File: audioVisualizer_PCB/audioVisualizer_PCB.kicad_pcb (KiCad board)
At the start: 2 copper layers, 129.1 x 32.5 mm, 34 parts, among them J1 USB_C_Receptacle_USB2.0_16P, J3 SPI_LED_MATRIX, U2 HT7333, U7 STM32F401CCUx, Y1 ASE-25MHz

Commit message: reflect on code as well
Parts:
- renumbered TP2 to 3V3, TP1 to 5V1, TP5 to GND1
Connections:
- J3 pad 4: Net-(J3-CS) -> SPI_CS
- U7 pad 16: Net-(J3-CS) -> unconnected-(U7-PA6-Pad16)
- U7 pad 27: unconnected-(U7-PB14-Pad27) -> SPI_CS
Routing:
- net SPI_CS: track 0.00 -> 66.5 mm
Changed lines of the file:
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@@
 			(layers "*.Cu" "*.Mask")
 			(remove_unused_layers no)
-			(net "Net-(J3-CS)")
+			(net "SPI_CS")
 			(pinfunction "CS_4")
 			(pintype "passive")
@@
 			(layers "F.Cu" "F.Mask" "F.Paste")
 			(roundrect_rratio 0.25)
-			(net "Net-(J3-CS)")
+			(net "unconnected-(U7-PA6-Pad16)")
 			(pinfunction "PA6_16")
 			(pintype "bidirectional")
@@
 			(layers "F.Cu" "F.Mask" "F.Paste")
 			(roundrect_rratio 0.25)
-			(net "unconnected-(U7-PB14-Pad27)")
+			(net "SPI_CS")
 			(pinfunction "PB14_27")
 			(pintype "bidirectional")
@@
 		(descr "SMD rectangular pad as test Point, square 1.0mm side length")
 		(tags "test point SMD pad rectangle square")
-		(property "Reference" "TP1"
+		(property "Reference" "5V1"
 			(at 0 1.448 0)
 			(layer "B.SilkS")
@@
 		(descr "SMD rectangular pad as test Point, square 1.0mm side length")
 		(tags "test point SMD pad rectangle square")
-		(property "Reference" "TP2"
+		(property "Reference" "3V3"
 			(at 0 1.448 0)
 			(layer "B.SilkS")
@@
 		(descr "SMD rectangular pad as test Point, square 1.0mm side length")
 		(tags "test point SMD pad rectangle square")
-		(property "Reference" "TP5"
+		(property "Reference" "GND1"
 			(at 0 1.448 0)
 			(layer "B.SilkS")
@@
 	(segment
 		(start 81.6245 88.2832)
-		(end 81.6245 88.7666)
+		(end 81.6245 89.1245)
 		(width 0.2)
 		(layer "F.Cu")
@@
 	)
 	(segment
-		(start 82.8328 89.9749)
+		(start 82.4749 89.9749)
 		(end 145.6851 89.9749)
 		(width 0.2)
@@
 	)
 	(segment
-		(start 81.6245 88.7666)
-		(end 82.8328 89.9749)
+		(start 81.6245 89.1245)
+		(end 82.4749 89.9749)
 		(width 0.2)
 		(layer "F.Cu")
@@
 		(net "Net-(J1-CC2)")
 	)
+	(segment
+		(start 145.223654 83.73)
+		(end 146.176346 83.73)
+		(width 0.2)
+		(layer "F.Cu")
+		(net "SPI_CS")
+	)
+	(segment
+		(start 89.553571 88.4194)
+		(end 140.534254 88.4194)
+		(width 0.2)
+		(layer "F.Cu")
+		(net "SPI_CS")
+	)
+	(segment
+		(start 140.534254 88.4194)
+		(end 145.223654 83.73)
+		(width 0.2)
+		(layer "F.Cu")
+		(net "SPI_CS")
+	)
+	(segment
+		(start 146.176346 83.73)
+		(end 146.85 84.403654)
+		(width 0.2)
+		(layer "F.Cu")
+		(net "SPI_CS")
+	)
+	(segment
+		(start 146.85 86.27)
+		(end 145.7 87.42)
+		(width 0.2)
+		(layer "F.Cu")
+		(net "SPI_CS")
+	)
+	(segment
+		(start 87.729871 86.5957)
+		(end 89.553571 88.4194)
+		(width 0.2)
+		(layer "F.Cu")
+		(net "SPI_CS")
+	)
+	(segment
+		(start 146.85 84.403654)
+		(end 146.85 86.27)
+		(width 0.2)
+		(layer "F.Cu")
+		(net "SPI_CS")
+	)
+	(segment
+		(start 86.812 86.5957)
+		(end 87.729871 86.5957)
+		(width 0.2)
+		(layer "F.Cu")
+		(net "SPI_CS")
+	)
 	(embedded_fonts no)

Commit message: update
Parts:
- removed TP3: SWDIO, TestPoint:TestPoint_Pad_1.0x1.0mm
- removed TP4: SWCLK, TestPoint:TestPoint_Pad_1.0x1.0mm
- added D2: LED, LED_SMD:LED_0805_2012Metric, F.Cu at (48.3, 96.0)
- added J2: SWD_DEBUG, Connector_PinHeader_2.54mm:PinHeader_1x04_P2.54mm_Vertical, F.Cu at (94.1, 70.5)
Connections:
- U7 pad 34: Net-(U7-PA13) -> SWDIO
- U7 pad 37: Net-(U7-PA14) -> SWCLK
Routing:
- net +5V: track 173.9 -> 216.9 mm
- net GND: track 310.7 -> 275.9 mm, vias 3 -> 5
- net Net-(U7-PA13): track 21.5 -> 0.00 mm, vias 1 -> 0
- net +3.3V: track 210.9 -> 229.9 mm
- net SWDIO: track 0.00 -> 17.2 mm, vias 0 -> 1
- net Net-(U7-PA14): track 15.9 -> 0.00 mm, vias 1 -> 0
- net SWCLK: track 0.00 -> 14.1 mm, vias 0 -> 1
- added copper zone on B.Cu, net GND

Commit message: update
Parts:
- removed C1: 15pF, Capacitor_SMD:C_0805_2012Metric
- removed C10, C9: 1uF, Capacitor_SMD:C_0805_2012Metric
- removed C8: 10nF, Capacitor_SMD:C_0805_2012Metric
- removed U2: HT7333, Package_TO_SOT_SMD:SOT-89-3
- added C18: 100nF, Capacitor_SMD:C_0805_2012Metric, F.Cu at (21.2, 72.8)
- added C19: 2.2uF, Capacitor_SMD:C_0805_2012Metric, F.Cu at (86.0, 90.4)
- added C2: 100nF, Capacitor_SMD:C_0805_2012Metric, F.Cu at (136.1, 74.4)
- added C20: 100nF, Capacitor_SMD:C_0805_2012Metric, F.Cu at (89.6, 82.0)
- added D3: LED, LED_SMD:LED_0805_2012Metric, F.Cu at (110.2, 88.9)
- added R4: 10k, Resistor_SMD:R_0805_2012Metric, B.Cu at (91.2, 75.4)
- added R5: 10k, Resistor_SMD:R_0805_2012Metric, F.Cu at (85.7, 74.6)
- added R6: 100Ω, Resistor_SMD:R_0805_2012Metric, F.Cu at (110.2, 83.0)
- added R7: 10Ω, Resistor_SMD:R_0805_2012Metric, F.Cu at (110.2, 85.9)
- added U1: AMS1117-3.3, Package_TO_SOT_SMD:SOT-223-3_TabPin2, F.Cu at (58.1, 95.7)
- C7: value 10uF -> 4.7uF
- J1: value USB_C_Receptacle_USB2.0_16P -> USB_C_16P
- MK-L1: value INMP441-L -> INMP43434-L; footprint Custom:MIC_INMP441ACEZ-R7 -> Custom:MIC_ICS-43434
- MK-R1: value INMP441-R -> INMP43434-R; footprint Custom:MIC_INMP441ACEZ-R7 -> Custom:MIC_ICS-43434
- R2: value 10 -> 10Ω
- Y1: footprint Oscillator:Oscillator_SMD_Abracon_ASE-4Pin_3.2x2.5mm -> Oscillator:Oscillator_SMD_EuroQuartz_XO32-4Pin_3.2x2.5mm
- moved C6 21.8 mm to (69.2, 80.7)
- moved C13 15.8 mm to (74.6, 94.2), turned to 180 degrees
- moved C5 3.27 mm to (76.6, 82.8), turned to -90 degrees
- moved MK-R1 3.14 mm to (140.2, 73.0), turned to 180 degrees
- moved MK-L1 3.03 mm to (25.8, 73.0), turned to 180 degrees
- moved C4 3.02 mm to (88.8, 89.6), turned to -90 degrees
- moved C7 1.66 mm to (96.2, 80.0)
- moved Y1 1.56 mm to (68.4, 86.3)
- moved 5V1 1.52 mm to (41.6, 98.4)
- moved C3 1.43 mm to (80.6, 78.7), turned to 90 degrees
- moved C17 1.10 mm to (126.4, 80.0)
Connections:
- net Net-(J3-CLK) renamed SPI_CLK
- net Net-(J3-DIN) renamed SPI_DIN
- net Net-(U7-PH0) renamed /CRYS_OUT
- C6 pad 1: +3.3V -> GND
- C6 pad 2: GND -> +3.3V
- D2 pad 1: GND -> Net-(D2-K)
- MK-L1 pad 1: MIC_SCK -> MIC_WS
- MK-L1 pad 2: MIC_WS -> GND
- MK-L1 pad 3: MIC_SD -> GND
- MK-L1 pad 4: GND -> MIC_SCK
- MK-L1 pad 5: GND -> +3.3V
- MK-L1 pad 6: GND -> MIC_SD
- MK-R1 pad 1: MIC_SCK -> MIC_WS
- MK-R1 pad 2: MIC_WS -> +3.3V
- MK-R1 pad 3: MIC_SD -> GND
- MK-R1 pad 4: +3.3V -> MIC_SCK
- MK-R1 pad 5: GND -> +3.3V
- MK-R1 pad 6: GND -> MIC_SD
- R29 pad 1: MIC_WS -> MIC_SD
- U7 pad 13: unconnected-(U7-PA3-Pad13) -> Net-(D3-A)
- U7 pad 22: unconnected-(U7-VCAP1-Pad22) -> Net-(U7-VCAP1)
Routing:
- net GND: track 275.9 -> 0.00 mm, vias 5 -> 0
- net +3.3V: track 229.9 -> 0.00 mm, vias 5 -> 0
- net +5V: track 216.9 -> 0.00 mm, vias 3 -> 0
- net MIC_SCK: track 134.0 -> 0.00 mm, vias 3 -> 0
- net MIC_SD: track 131.1 -> 0.00 mm, vias 3 -> 0
- net MIC_WS: track 126.8 -> 0.00 mm, vias 3 -> 0
- net USB_DP: track 79.0 -> 0.00 mm, vias 1 -> 0
- net USB_DM: track 77.4 -> 0.00 mm, vias 1 -> 0
- net SPI_CS: track 66.5 -> 0.00 mm
- net SPI_DIN: track 65.8 -> 0.00 mm
- net SPI_CLK: track 65.3 -> 0.00 mm
- net SWDIO: track 17.2 -> 0.00 mm, vias 1 -> 0
- net SWCLK: track 14.1 -> 0.00 mm, vias 1 -> 0
- net Net-(U7-NRST): track 12.0 -> 0.00 mm, vias 2 -> 0
- net /CRYS_OUT: track 9.66 -> 0.00 mm
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
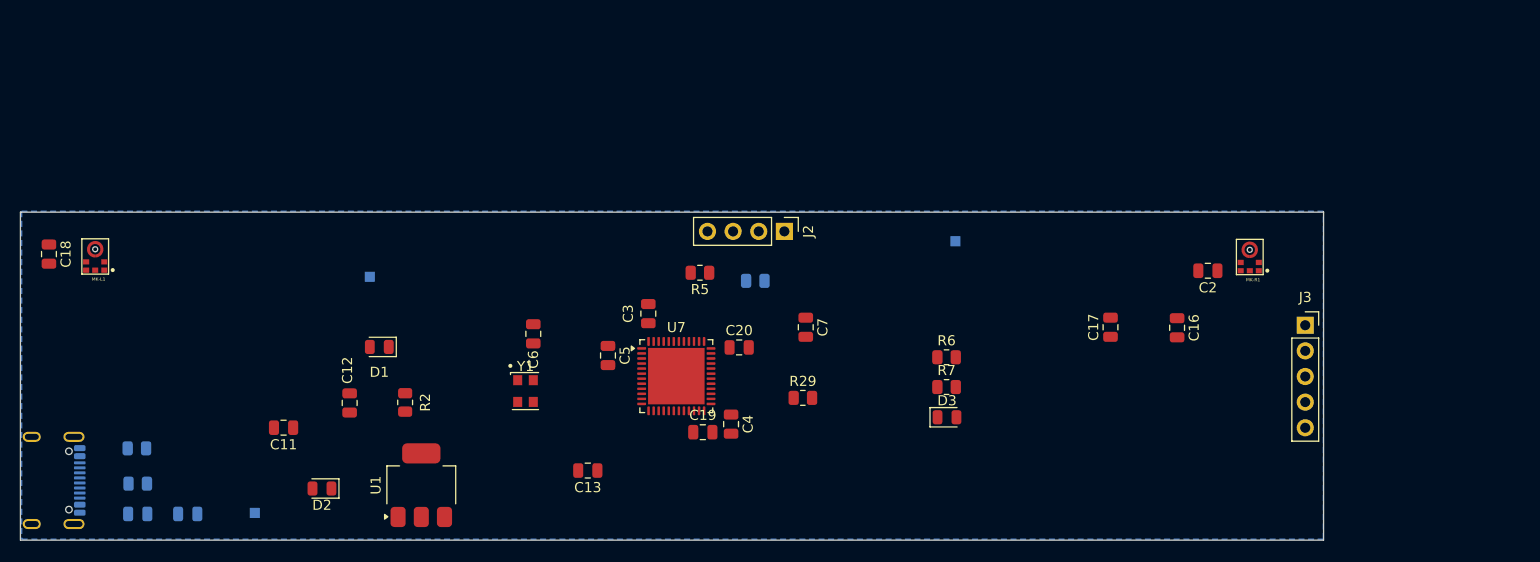
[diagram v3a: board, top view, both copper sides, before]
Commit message: manually routed the tracks; switch LEFT/RIGHT mic
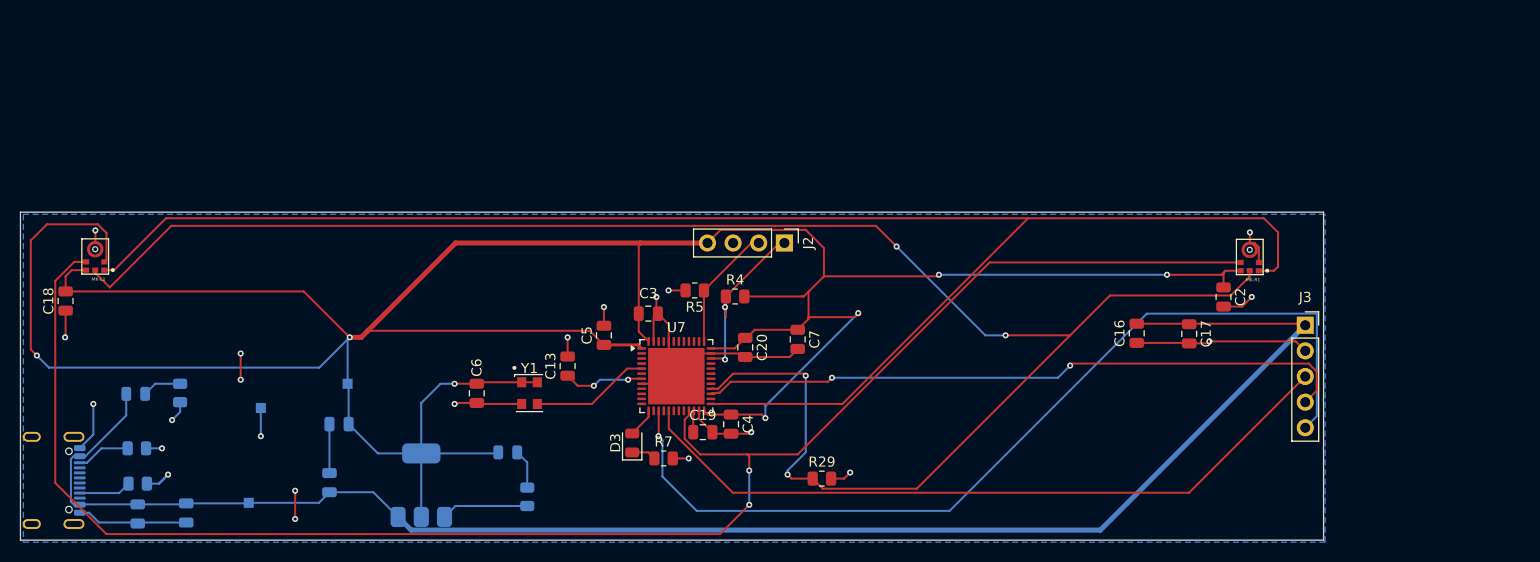
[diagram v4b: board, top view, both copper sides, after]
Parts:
- C11, C12: value 10u -> 10uF; moved to B.Cu
- D1, D2, R2, R6, U1: moved to B.Cu
- R4: moved to F.Cu
- moved R6 76.0 mm to (34.2, 86.5), turned to -90 degrees
- moved GND1 70.8 mm to (42.2, 88.0)
- moved D3 31.3 mm to (79.0, 91.5), turned to 90 degrees
- moved R7 28.9 mm to (82.1, 93.0)
- moved D2 20.7 mm to (29.8, 86.6)
- moved D1 16.5 mm to (66.7, 92.4)
- moved R2 15.3 mm to (68.6, 96.8)
- moved 3V3 10.8 mm to (50.8, 85.6)
- moved C13 10.5 mm to (72.6, 83.8), turned to 90 degrees
- moved R29 8.22 mm to (97.8, 95.0)
- moved C6 8.13 mm to (63.6, 86.5), turned to 90 degrees
- moved C17 7.83 mm to (134.2, 80.7), turned to -90 degrees
- moved C11 7.10 mm to (49.0, 95.4), turned to 90 degrees
- moved C18 4.93 mm to (22.9, 77.4), turned to 90 degrees
- moved C16 4.04 mm to (129.0, 80.6), turned to 90 degrees
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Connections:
- J1 pad A6: USB_DP -> unconnected-(J1-D+-PadA6)
- J1 pad A7: USB_DM -> unconnected-(J1-D--PadA7)
- J1 pad B6: USB_DP -> unconnected-(J1-D+-PadA6)
- J1 pad B7: USB_DM -> unconnected-(J1-D--PadA7)
- MK-L1 pad 2: GND -> +3.3V
- MK-R1 pad 2: +3.3V -> GND
- U7 pad 32: USB_DM -> unconnected-(U7-PA11-Pad32)
- U7 pad 33: USB_DP -> unconnected-(U7-PA12-Pad33)
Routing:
- net +3.3V: track 0.00 -> 322.1 mm, vias 0 -> 7
- net MIC_SD: track 0.00 -> 180.8 mm, vias 0 -> 4
- net MIC_SCK: track 0.00 -> 167.6 mm, vias 0 -> 2
- net MIC_WS: track 0.00 -> 163.5 mm
- net +5V: track 0.00 -> 163.4 mm
- net GND: track 0.00 -> 124.1 mm, vias 0 -> 22
- net SPI_CLK: track 0.00 -> 92.8 mm, vias 0 -> 1
- net SPI_DIN: track 0.00 -> 72.2 mm
- net SPI_CS: track 0.00 -> 65.1 mm, vias 0 -> 2
- net SWDIO: track 0.00 -> 16.9 mm, vias 0 -> 2
- net SWCLK: track 0.00 -> 12.5 mm
- net /CRYS_OUT: track 0.00 -> 11.8 mm
- net Net-(U7-NRST): track 0.00 -> 8.04 mm, vias 0 -> 2
- net Net-(J1-CC2): track 0.00 -> 5.34 mm
- net Net-(J1-CC1): track 0.00 -> 5.22 mm
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
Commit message: added cap for vref pin
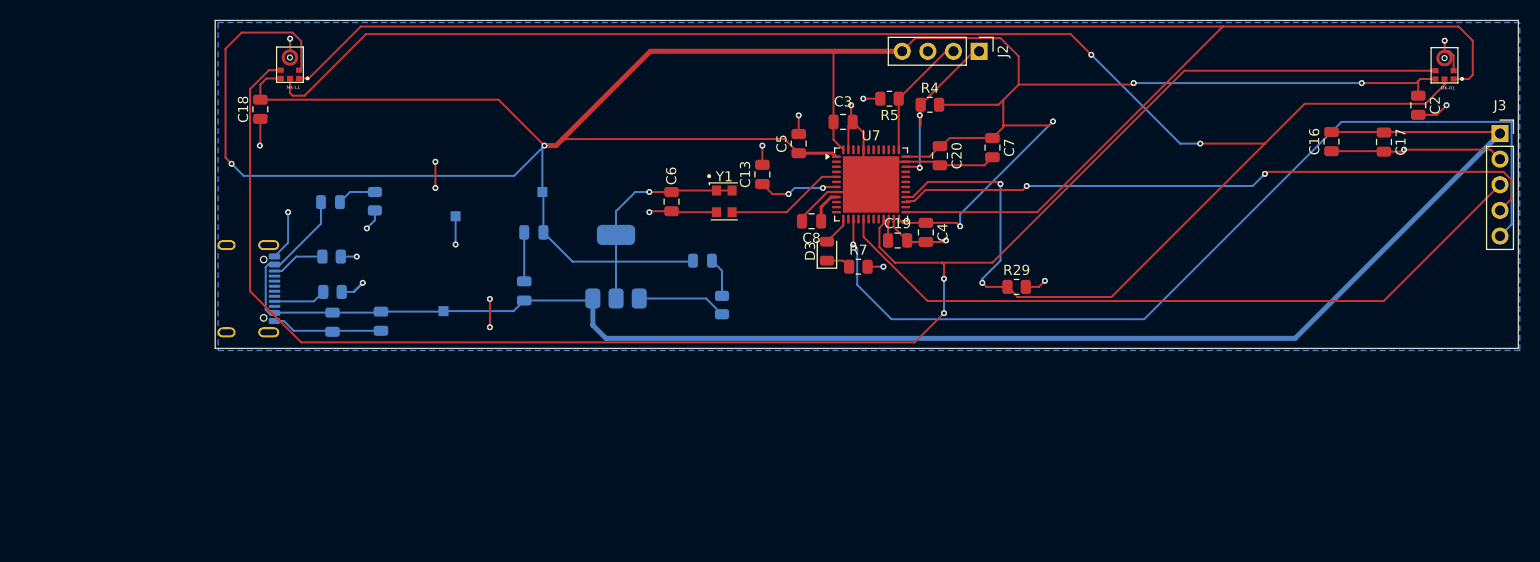
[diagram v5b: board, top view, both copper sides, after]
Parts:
- added C8: 100nF, Capacitor_SMD:C_0805_2012Metric, F.Cu at (96.8, 69.5)
- MK-L1: value INMP43434-L -> INMP43434-R
- MK-R1: value INMP43434-R -> INMP43434-L
- moved U1 29.0 mm to (77.4, 74.0)
- moved C17 27.1 mm to (153.5, 61.6)
- moved C3 27.1 mm to (99.9, 59.6)
- moved C13 27.1 mm to (91.9, 64.8)
- moved C2 27.1 mm to (156.9, 58.0)
- moved D1 27.1 mm to (86.0, 73.4)
- moved J3 27.1 mm to (165.0, 60.8)
- moved MK-R1 27.1 mm to (159.5, 54.0)
- moved R2 27.1 mm to (87.9, 77.8)
- moved kibuzzard-69F6314F 27.1 mm to (146.8, 52.5)
- moved C15 27.1 mm to (54.1, 79.4)
- moved C16 27.1 mm to (148.3, 61.6)
- moved C18 27.1 mm to (42.1, 58.4)
- moved C6 27.1 mm to (82.9, 67.5)
- moved J2 27.1 mm to (113.4, 52.6)
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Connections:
- U7 pad 9: unconnected-(U7-VREF+-Pad9) -> +3.3V
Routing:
- net GND: track 124.1 -> 129.1 mm
- net +5V: track 163.4 -> 165.1 mm
- net +3.3V: track 322.1 -> 322.8 mm
- net MIC_SD: track 180.8 -> 181.5 mm
